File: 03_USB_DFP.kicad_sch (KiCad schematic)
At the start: 44 parts, among them U10 TPS20xxC, U11 USB_3_Type_A_Molex_484080003, U12 TPS20xxC, U13 USB_3_Type_A_Molex_484080003, U14 TPS20xxC, U15 USB_3_Type_A_Molex_484080003, U8 USB_3_Type_A_Molex_484080003, U9 TPS20xxC

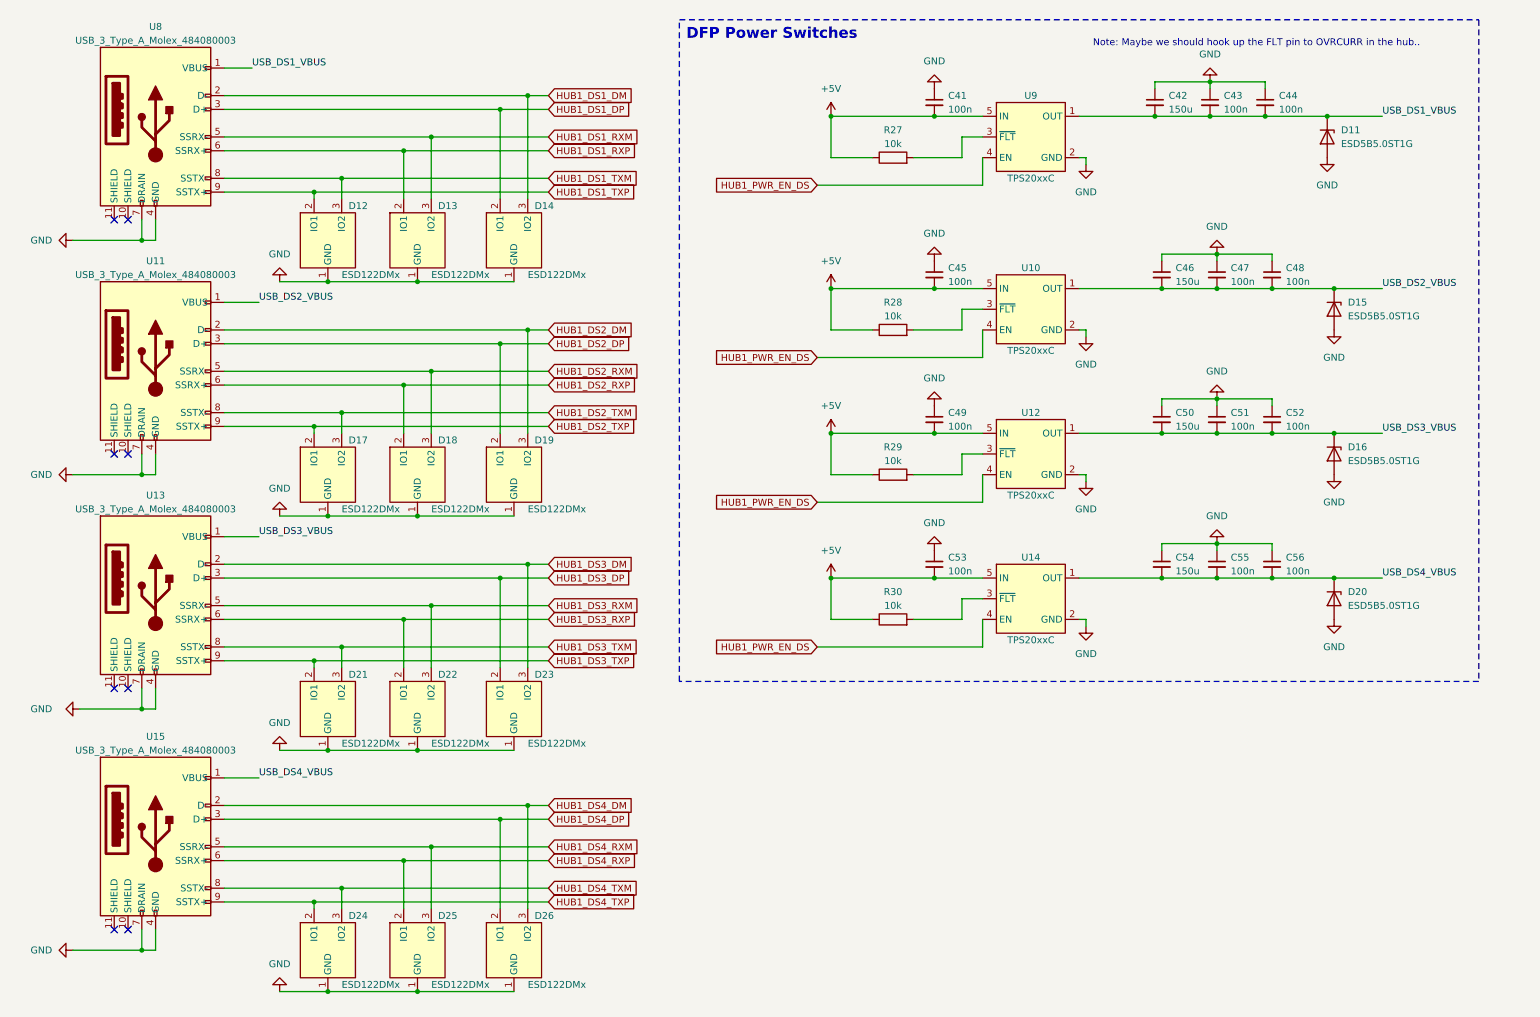
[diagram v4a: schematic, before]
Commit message: symbol fixes, switch ESD protection for USB datalines
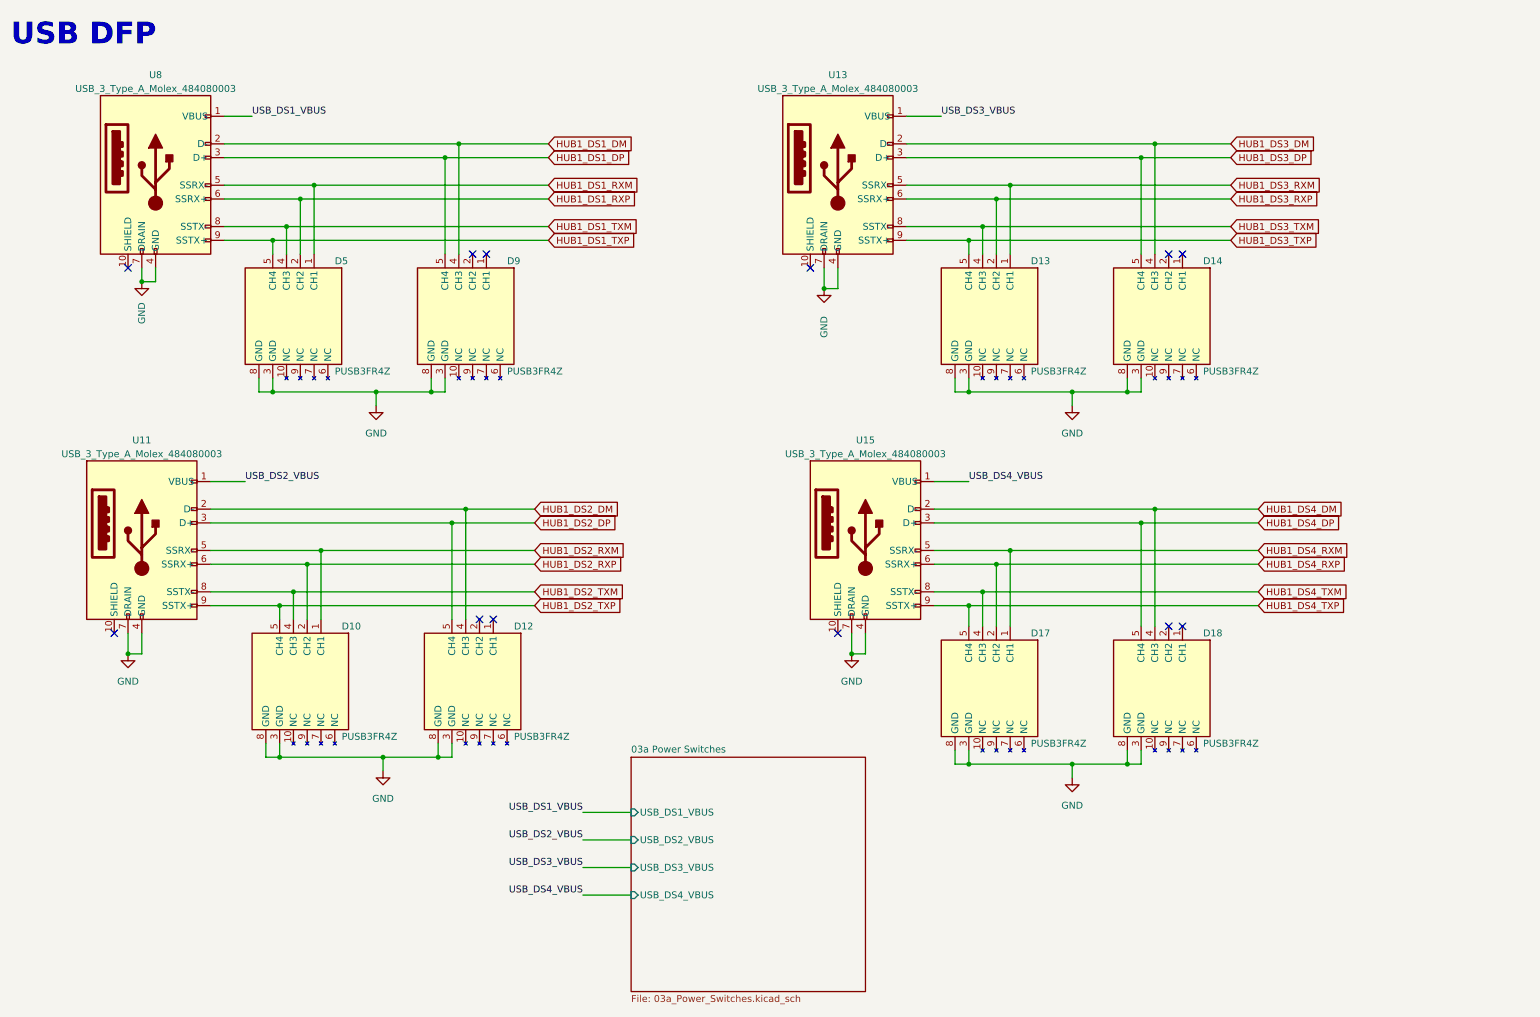
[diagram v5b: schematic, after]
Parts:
- removed C41, C43, C44, C45, C47, C48, C49, C51, C52, C53, C55, C56: 100n, Capacitor_SMD:C_0603_1608Metric, symbol Device:C_Small
- removed C42, C46, C50, C54: 150u, Capacitor_SMD:C_Elec_6.3x7.7, symbol Device:C_Small
- removed D11, D15, D16, D20: ESD5B5.0ST1G, Diode_SMD:D_SOD-523, symbol Device:D_Zener
- removed D12, D13, D14, D17, D18, D19, D21, D22, D23, D24, D25, D26: ESD122DMx, Cake_USB:ESD122DMX, symbol CakeUSB:ESD122DMx
- removed R27, R28, R29, R30: 10k, Resistor_SMD:R_0603_1608Metric, symbol Device:R
- removed U10, U12, U14, U9: TPS20xxC, Package_TO_SOT_SMD:SOT-23-5, symbol CakeUSB:TPS20xxC
- added D10, D12, D13, D14, D17, D18, D5, D9: PUSB3FR4Z, CakeUSB:PUSB3FR4Z, symbol CakeUSB:PUSB3FR4Z
- U11, U13, U15, U8: footprint Cake_USB:Molex_484080003 -> CakeUSB:Molex_484080003
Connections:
- net GND: now also D10.3 (GND), D10.8 (GND), D12.3 (GND), D12.8 (GND), D13.3 (GND), D13.8 (GND), D14.3 (GND), D14.8 (GND), D17.3 (GND), D17.8 (GND), D18.3 (GND), D18.8 (GND), D5.3 (GND), D5.8 (GND), D9.3 (GND), D9.8 (GND)
- net HUB1_DS1_DM: now also D9.4 (CH3)
- net HUB1_DS1_DP: now also D9.5 (CH4)
- net HUB1_DS1_RXM: now also D5.1 (CH1)
- net HUB1_DS1_RXP: now also D5.2 (CH2)
- net HUB1_DS1_TXM: now also D5.4 (CH3)
- net HUB1_DS1_TXP: now also D5.5 (CH4)
- net HUB1_DS2_DM: now also D12.4 (CH3)
- net HUB1_DS2_DP: now also D12.5 (CH4)
- net HUB1_DS2_RXM: now also D10.1 (CH1)
- net HUB1_DS2_RXP: now also D10.2 (CH2)
- net HUB1_DS2_TXM: now also D10.4 (CH3)
- net HUB1_DS2_TXP: now also D10.5 (CH4)
- net HUB1_DS3_DM: now also D14.4 (CH3)
- net HUB1_DS3_DP: now also D14.5 (CH4)
- net HUB1_DS3_RXM: now also D13.1 (CH1)
- net HUB1_DS3_RXP: now also D13.2 (CH2)
- net HUB1_DS3_TXM: now also D13.4 (CH3)
- net HUB1_DS3_TXP: now also D13.5 (CH4)
- net HUB1_DS4_DM: now also D18.4 (CH3)
- net HUB1_DS4_DP: now also D18.5 (CH4)
- net HUB1_DS4_RXM: now also D17.1 (CH1)
- net HUB1_DS4_RXP: now also D17.2 (CH2)
- net HUB1_DS4_TXM: now also D17.4 (CH3)
- net HUB1_DS4_TXP: now also D17.5 (CH4)
- no-connect marks 8 -> 12
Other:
- added sheet 03a Power Switches (03a_Power_Switches.kicad_sch)
- note added: "USB DFP"
- note removed: "DFP Power Switches"
- note removed: "Note: Maybe we should hook up the FLT pin to OVRCURR in the hub.."

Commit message: add RTL8153
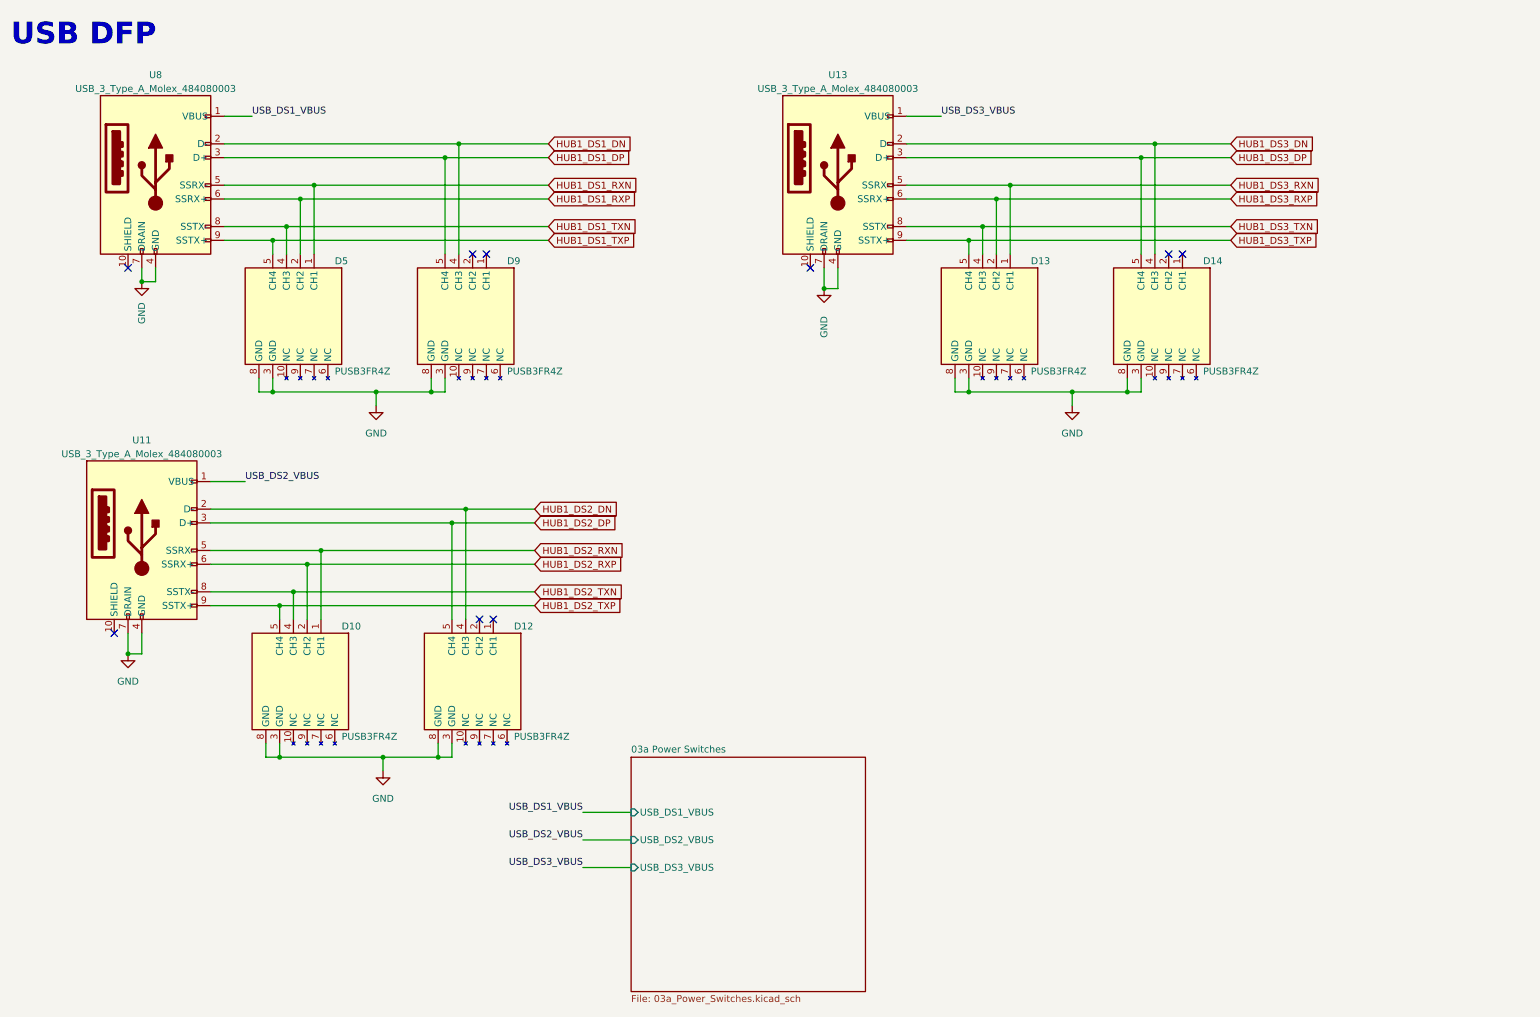
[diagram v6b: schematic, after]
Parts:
- removed D17, D18: PUSB3FR4Z, CakeUSB:PUSB3FR4Z, symbol CakeUSB:PUSB3FR4Z
- removed U15: USB_3_Type_A_Molex_484080003, CakeUSB:Molex_484080003, symbol CakeUSB:USB_3_Type_A_Molex_484080003
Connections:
- net HUB1_DS1_DM renamed HUB1_DS1_DN
- net HUB1_DS1_RXM renamed HUB1_DS1_RXN
- net HUB1_DS1_TXM renamed HUB1_DS1_TXN
- net HUB1_DS2_DM renamed HUB1_DS2_DN
- net HUB1_DS2_RXM renamed HUB1_DS2_RXN
- net HUB1_DS2_TXM renamed HUB1_DS2_TXN
- net HUB1_DS3_DM renamed HUB1_DS3_DN
- net HUB1_DS3_RXM renamed HUB1_DS3_RXN
- net HUB1_DS3_TXM renamed HUB1_DS3_TXN
- no-connect marks 12 -> 9
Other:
- sheet 03a Power Switches ports: added none; removed USB_DS4_VBUS

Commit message: route power delivery controller
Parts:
- renumbered D13 to D10, D14 to D11, D10 to D12, D12 to D13, D5 to D8, U11 to U10, U13 to U9
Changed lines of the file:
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@@
   (symbol (lib_id "CakeUSB:USB_3_Type_A_Molex_484080003") (at 165.1 41.91 0) (unit 1)
     (in_bom yes) (on_board yes) (dnp no)
-    (property "Reference" "U13" (at 165.1 24.13 0)
+    (property "Reference" "U9" (at 165.1 24.13 0)
       (effects (font (size 1.27 1.27)))
     )
@@
       (project "USBHUB"
         (path "/d5edc647-9ac3-4ac1-ab8a-57c77be3f4d3/aef239ad-726b-4cbb-b085-3b57a4599b3b"
-          (reference "U13") (unit 1)
+          (reference "U9") (unit 1)
         )
       )
@@
   (symbol (lib_id "CakeUSB:PUSB3FR4Z") (at 97.79 135.89 270) (unit 1)
     (in_bom yes) (on_board yes) (dnp no)
-    (property "Reference" "D12" (at 105.41 125.73 90)
+    (property "Reference" "D13" (at 105.41 125.73 90)
       (effects (font (size 1.27 1.27)) (justify left))
     )
@@
       (project "USBHUB"
         (path "/d5edc647-9ac3-4ac1-ab8a-57c77be3f4d3/aef239ad-726b-4cbb-b085-3b57a4599b3b"
-          (reference "D12") (unit 1)
+          (reference "D13") (unit 1)
         )
       )
@@
   (symbol (lib_id "CakeUSB:PUSB3FR4Z") (at 193.04 68.58 270) (unit 1)
     (in_bom yes) (on_board yes) (dnp no)
-    (property "Reference" "D13" (at 200.66 58.42 90)
+    (property "Reference" "D10" (at 200.66 58.42 90)
       (effects (font (size 1.27 1.27)) (justify left))
     )
@@
       (project "USBHUB"
         (path "/d5edc647-9ac3-4ac1-ab8a-57c77be3f4d3/aef239ad-726b-4cbb-b085-3b57a4599b3b"
-          (reference "D13") (unit 1)
+          (reference "D10") (unit 1)
         )
       )
@@
   (symbol (lib_id "CakeUSB:PUSB3FR4Z") (at 64.77 68.58 270) (unit 1)
     (in_bom yes) (on_board yes) (dnp no)
-    (property "Reference" "D5" (at 72.39 58.42 90)
+    (property "Reference" "D8" (at 72.39 58.42 90)
       (effects (font (size 1.27 1.27)) (justify left))
     )
@@
       (project "USBHUB"
         (path "/d5edc647-9ac3-4ac1-ab8a-57c77be3f4d3/aef239ad-726b-4cbb-b085-3b57a4599b3b"
-          (reference "D5") (unit 1)
+          (reference "D8") (unit 1)
         )
       )
@@
   (symbol (lib_id "power:GND") (at 81.28 152.4 0) (unit 1)
     (in_bom yes) (on_board yes) (dnp no) (fields_autoplaced)
-    (property "Reference" "#PWR067" (at 81.28 158.75 0)
+    (property "Reference" "#PWR055" (at 81.28 158.75 0)
       (effects (font (size 1.27 1.27)) hide)
     )
@@
       (project "USBHUB"
         (path "/d5edc647-9ac3-4ac1-ab8a-57c77be3f4d3/aef239ad-726b-4cbb-b085-3b57a4599b3b"
-          (reference "#PWR067") (unit 1)
+          (reference "#PWR055") (unit 1)
         )
       )
@@
   (symbol (lib_id "power:GND") (at 34.29 130.81 0) (unit 1)
     (in_bom yes) (on_board yes) (dnp no) (fields_autoplaced)
-    (property "Reference" "#PWR064" (at 34.29 137.16 0)
+    (property "Reference" "#PWR054" (at 34.29 137.16 0)
       (effects (font (size 1.27 1.27)) hide)
     )
@@
       (project "USBHUB"
         (path "/d5edc647-9ac3-4ac1-ab8a-57c77be3f4d3/aef239ad-726b-4cbb-b085-3b57a4599b3b"
-          (reference "#PWR064") (unit 1)
+          (reference "#PWR054") (unit 1)
         )
       )
@@
   (symbol (lib_id "power:GND") (at 162.56 63.5 0) (unit 1)
     (in_bom yes) (on_board yes) (dnp no)
-    (property "Reference" "#PWR073" (at 162.56 69.85 0)
+    (property "Reference" "#PWR051" (at 162.56 69.85 0)
       (effects (font (size 1.27 1.27)) hide)
     )
@@
       (project "USBHUB"
         (path "/d5edc647-9ac3-4ac1-ab8a-57c77be3f4d3/aef239ad-726b-4cbb-b085-3b57a4599b3b"
-          (reference "#PWR073") (unit 1)
+          (reference "#PWR051") (unit 1)
         )
       )
@@
   (symbol (lib_id "CakeUSB:PUSB3FR4Z") (at 224.79 68.58 270) (unit 1)
     (in_bom yes) (on_board yes) (dnp no)
-    (property "Reference" "D14" (at 232.41 58.42 90)
+    (property "Reference" "D11" (at 232.41 58.42 90)
       (effects (font (size 1.27 1.27)) (justify left))
     )
@@
       (project "USBHUB"
         (path "/d5edc647-9ac3-4ac1-ab8a-57c77be3f4d3/aef239ad-726b-4cbb-b085-3b57a4599b3b"
-          (reference "D14") (unit 1)
+          (reference "D11") (unit 1)
         )
       )
@@
   (symbol (lib_id "CakeUSB:USB_3_Type_A_Molex_484080003") (at 36.83 109.22 0) (unit 1)
     (in_bom yes) (on_board yes) (dnp no)
-    (property "Reference" "U11" (at 36.83 91.44 0)
+    (property "Reference" "U10" (at 36.83 91.44 0)
       (effects (font (size 1.27 1.27)))
     )
@@
       (project "USBHUB"
         (path "/d5edc647-9ac3-4ac1-ab8a-57c77be3f4d3/aef239ad-726b-4cbb-b085-3b57a4599b3b"
-          (reference "U11") (unit 1)
+          (reference "U10") (unit 1)
         )
       )
@@
   (symbol (lib_id "power:GND") (at 208.28 85.09 0) (unit 1)
     (in_bom yes) (on_board yes) (dnp no) (fields_autoplaced)
-    (property "Reference" "#PWR048" (at 208.28 91.44 0)
+    (property "Reference" "#PWR053" (at 208.28 91.44 0)
       (effects (font (size 1.27 1.27)) hide)
     )
@@
       (project "USBHUB"
         (path "/d5edc647-9ac3-4ac1-ab8a-57c77be3f4d3/aef239ad-726b-4cbb-b085-3b57a4599b3b"
-          (reference "#PWR048") (unit 1)
+          (reference "#PWR053") (unit 1)
         )
       )
@@
   (symbol (lib_id "CakeUSB:PUSB3FR4Z") (at 66.04 135.89 270) (unit 1)
     (in_bom yes) (on_board yes) (dnp no)
-    (property "Reference" "D10" (at 73.66 125.73 90)
+    (property "Reference" "D12" (at 73.66 125.73 90)
       (effects (font (size 1.27 1.27)) (justify left))
     )
@@
       (project "USBHUB"
         (path "/d5edc647-9ac3-4ac1-ab8a-57c77be3f4d3/aef239ad-726b-4cbb-b085-3b57a4599b3b"
-          (reference "D10") (unit 1)
+          (reference "D12") (unit 1)
         )
       )
@@
   (symbol (lib_id "power:GND") (at 36.83 62.23 0) (unit 1)
     (in_bom yes) (on_board yes) (dnp no)
-    (property "Reference" "#PWR054" (at 36.83 68.58 0)
+    (property "Reference" "#PWR050" (at 36.83 68.58 0)
       (effects (font (size 1.27 1.27)) hide)
     )
@@
       (project "USBHUB"
         (path "/d5edc647-9ac3-4ac1-ab8a-57c77be3f4d3/aef239ad-726b-4cbb-b085-3b57a4599b3b"
-          (reference "#PWR054") (unit 1)
+          (reference "#PWR050") (unit 1)
         )
       )
@@
   (symbol (lib_id "power:GND") (at 80.01 85.09 0) (unit 1)
     (in_bom yes) (on_board yes) (dnp no) (fields_autoplaced)
-    (property "Reference" "#PWR057" (at 80.01 91.44 0)
+    (property "Reference" "#PWR052" (at 80.01 91.44 0)
       (effects (font (size 1.27 1.27)) hide)
     )
@@
       (project "USBHUB"
         (path "/d5edc647-9ac3-4ac1-ab8a-57c77be3f4d3/aef239ad-726b-4cbb-b085-3b57a4599b3b"
-          (reference "#PWR057") (unit 1)
-        )
-      )
+          (reference "#PWR052") (unit 1)
+        )
+      )

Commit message: finish layout draft
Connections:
- net HUB1_DS3_DN: now also D11.1 (CH1); no longer D11.4 (CH3)
- net HUB1_DS3_DP: now also D11.2 (CH2); no longer D11.5 (CH4)
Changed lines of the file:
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@@
   (junction (at 67.31 114.3) (diameter 0) (color 0 0 0 0)
   )
-  (junction (at 223.52 36.83) (diameter 0) (color 0 0 0 0)
+  (junction (at 228.6 36.83) (diameter 0) (color 0 0 0 0)
   )
   (junction (at 66.04 46.99) (diameter 0) (color 0 0 0 0)
@@
   (junction (at 68.58 44.45) (diameter 0) (color 0 0 0 0)
   )
-  (junction (at 220.98 39.37) (diameter 0) (color 0 0 0 0)
-  )
   (junction (at 95.25 36.83) (diameter 0) (color 0 0 0 0)
   )
@@
   )
   (junction (at 63.5 52.07) (diameter 0) (color 0 0 0 0)
+  )
+  (junction (at 226.06 39.37) (diameter 0) (color 0 0 0 0)
   )
   (junction (at 60.96 82.55) (diameter 0) (color 0 0 0 0)
@@
   (no_connect (at 34.29 59.69))
   (no_connect (at 101.6 124.46))
-  (no_connect (at 226.06 57.15))
-  (no_connect (at 228.6 57.15))
   (no_connect (at 97.79 57.15))
+  (no_connect (at 223.52 57.15))
   (no_connect (at 31.75 127))
   (no_connect (at 99.06 124.46))
   (no_connect (at 160.02 59.69))
+  (no_connect (at 220.98 57.15))
   (no_connect (at 100.33 57.15))
   (wire (pts (xy 189.23 54.61) (xy 189.23 57.15))
@@
     (stroke (width 0) (type default))
   )
-  (wire (pts (xy 220.98 39.37) (xy 220.98 57.15))
-    (stroke (width 0) (type default))
-  )
   (wire (pts (xy 95.25 36.83) (xy 111.76 36.83))
     (stroke (width 0) (type default))
@@
     (stroke (width 0) (type default))
   )
+  (wire (pts (xy 228.6 36.83) (xy 228.6 57.15))
+    (stroke (width 0) (type default))
+  )
   (wire (pts (xy 218.44 82.55) (xy 208.28 82.55))
     (stroke (width 0) (type default))
   )
-  (wire (pts (xy 223.52 57.15) (xy 223.52 36.83))
-    (stroke (width 0) (type default))
-  )
-  (wire (pts (xy 220.98 39.37) (xy 237.49 39.37))
-    (stroke (width 0) (type default))
-  )
-  (wire (pts (xy 223.52 36.83) (xy 237.49 36.83))
+  (wire (pts (xy 177.8 36.83) (xy 228.6 36.83))
     (stroke (width 0) (type default))
   )
@@
     (stroke (width 0) (type default))
   )
+  (wire (pts (xy 226.06 57.15) (xy 226.06 39.37))
+    (stroke (width 0) (type default))
+  )
   (wire (pts (xy 34.29 127) (xy 34.29 130.81))
     (stroke (width 0) (type default))
@@
     (stroke (width 0) (type default))
   )
+  (wire (pts (xy 226.06 39.37) (xy 237.49 39.37))
+    (stroke (width 0) (type default))
+  )
   (wire (pts (xy 60.96 82.55) (xy 80.01 82.55))
     (stroke (width 0) (type default))
@@
     (stroke (width 0) (type default))
   )
-  (wire (pts (xy 177.8 36.83) (xy 223.52 36.83))
+  (wire (pts (xy 228.6 36.83) (xy 237.49 36.83))
     (stroke (width 0) (type default))
   )
@@
     (stroke (width 0) (type default))
   )
-  (wire (pts (xy 177.8 39.37) (xy 220.98 39.37))
-    (stroke (width 0) (type default))
-  )
+  (wire (pts (xy 177.8 39.37) (xy 226.06 39.37))
+    (stroke (width 0) (type default))
+  )
